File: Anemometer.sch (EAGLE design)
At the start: 30 parts, among them IC1 TINY2313-*S*, IC2 74HC151D, IC3 74HC151D, IC4 74HC08D, IC5 LM555D, IC6 74HC138D, IC7 74ALS04D, IC8 74HC393D, Q1 16MHz

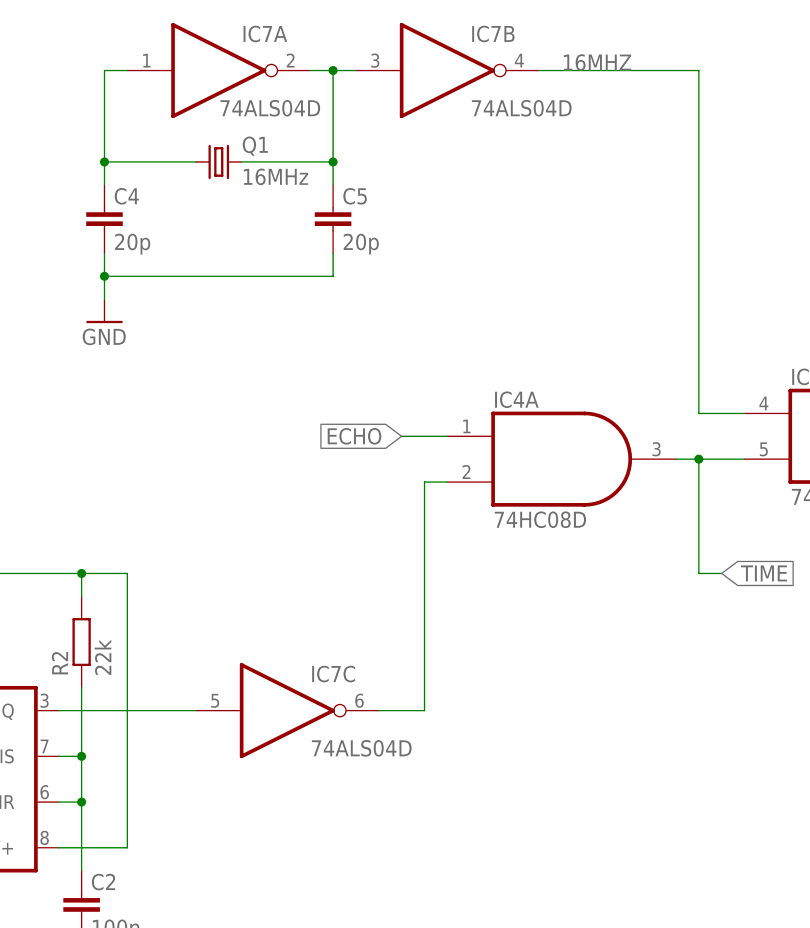
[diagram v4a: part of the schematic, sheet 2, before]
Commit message: added timeout protection
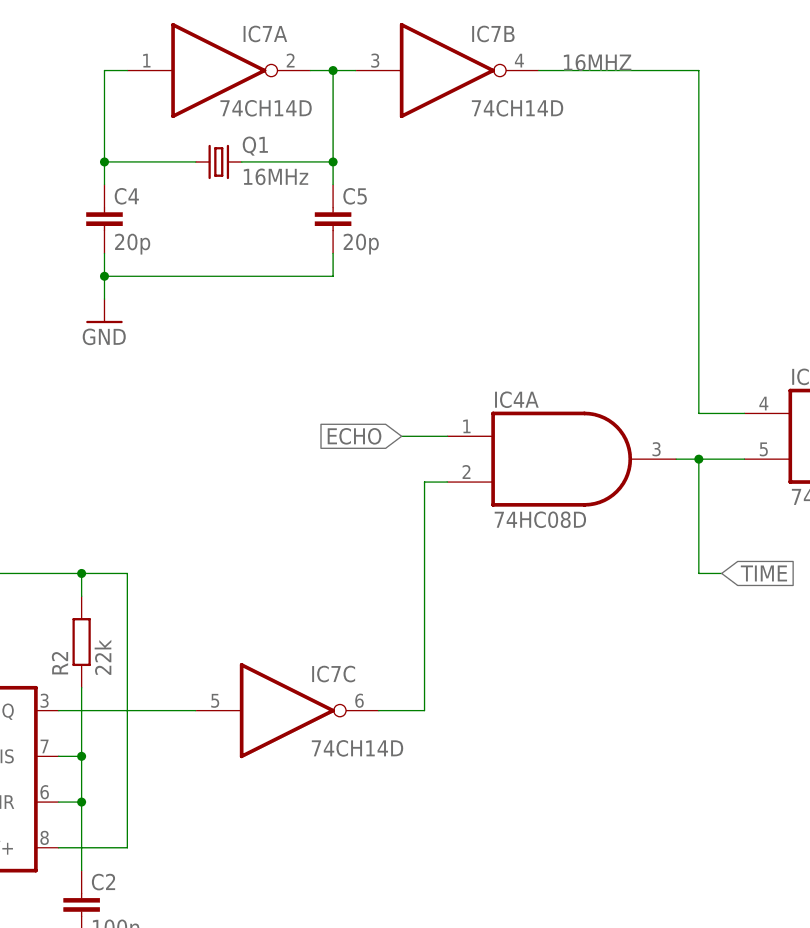
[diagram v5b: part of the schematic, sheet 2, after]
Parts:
- IC7: value 74ALS04D -> 74CH14D
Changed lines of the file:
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@@
 <part name="FRAME4" library="frames" library_urn="urn:adsk.eagle:library:229" deviceset="A4L-LOC" device="" value="Frame"/>
 <part name="IC8" library="74xx-us" library_urn="urn:adsk.eagle:library:88" deviceset="74*393" device="D" package3d_urn="urn:adsk.eagle:package:2917/1" technology="LS" value="74HC393D"/>
-<part name="IC7" library="74xx-us" library_urn="urn:adsk.eagle:library:88" deviceset="74*04" device="D" package3d_urn="urn:adsk.eagle:package:2917/1" technology="ALS"/>
+<part name="IC7" library="74xx-us" library_urn="urn:adsk.eagle:library:88" deviceset="74*04" device="D" package3d_urn="urn:adsk.eagle:package:2917/1" technology="ALS" value="74CH14D"/>
 <part name="P+12" library="supply1" library_urn="urn:adsk.eagle:library:371" deviceset="VCC" device=""/>
 <part name="GND16" library="supply1" library_urn="urn:adsk.eagle:library:371" deviceset="GND" device=""/>

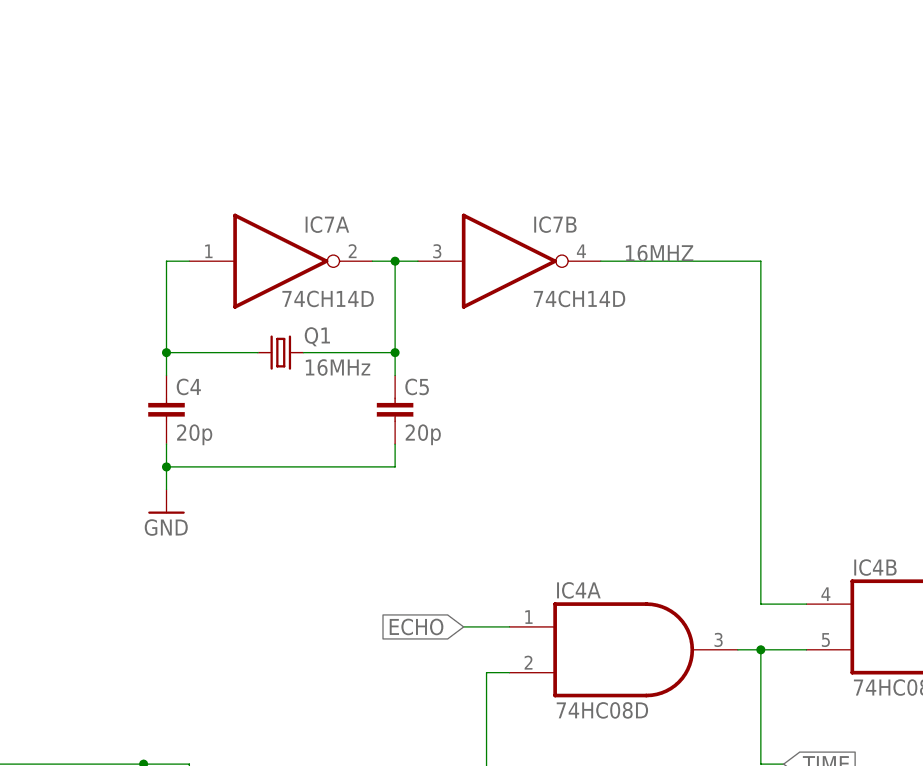
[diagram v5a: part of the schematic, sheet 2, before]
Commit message: added resistors to make clock run reliable
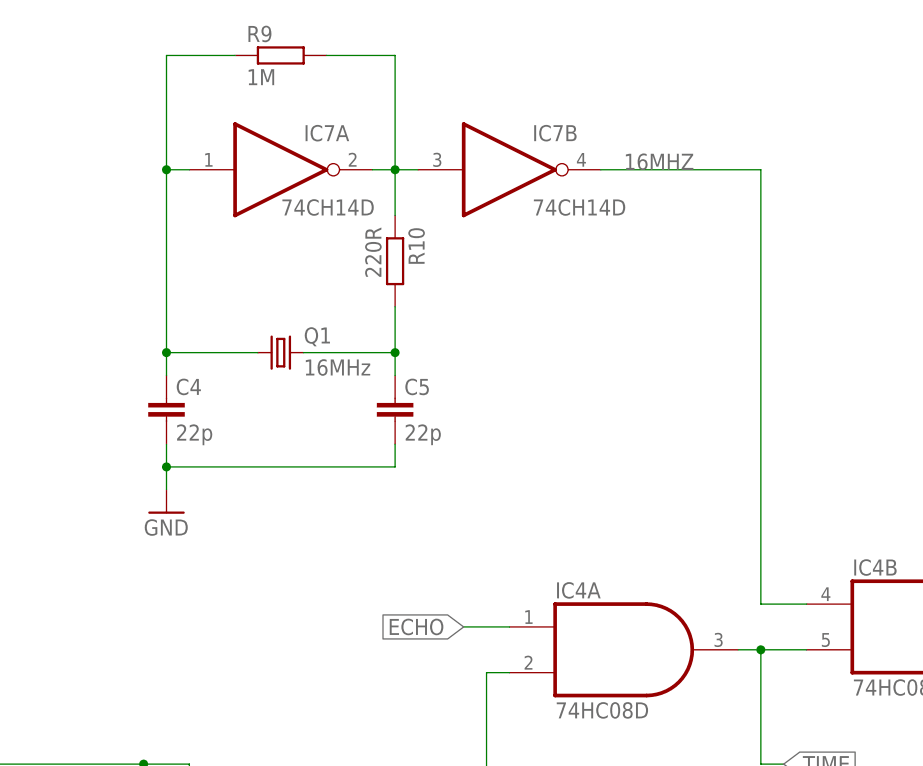
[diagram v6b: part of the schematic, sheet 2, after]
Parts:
- added R10: 220R, rcl:R-EU_R0805
- added R9: 1M, rcl:R-EU_R0805
- C4, C5: value 20p -> 22p
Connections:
- new net N$8: IC7A.O, IC7B.I, R10.1, R9.2
- net N$6: now also R9.1
- net N$7: now also R10.2; no longer IC7A.O, IC7B.I
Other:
- moved on the sheet: IC7A, IC7B
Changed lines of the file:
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@@
 <part name="GND14" library="supply1" library_urn="urn:adsk.eagle:library:371" deviceset="GND" device=""/>
 <part name="Q1" library="crystal" library_urn="urn:adsk.eagle:library:204" deviceset="CRYSTAL" device="HC49UP" package3d_urn="urn:adsk.eagle:package:12078/1" value="16MHz"/>
-<part name="C4" library="rcl" library_urn="urn:adsk.eagle:library:334" deviceset="C-EU" device="C0805" package3d_urn="urn:adsk.eagle:package:23617/2" value="20p"/>
-<part name="C5" library="rcl" library_urn="urn:adsk.eagle:library:334" deviceset="C-EU" device="C0805" package3d_urn="urn:adsk.eagle:package:23617/2" value="20p"/>
+<part name="C4" library="rcl" library_urn="urn:adsk.eagle:library:334" deviceset="C-EU" device="C0805" package3d_urn="urn:adsk.eagle:package:23617/2" value="22p"/>
+<part name="C5" library="rcl" library_urn="urn:adsk.eagle:library:334" deviceset="C-EU" device="C0805" package3d_urn="urn:adsk.eagle:package:23617/2" value="22p"/>
 <part name="GND15" library="supply1" library_urn="urn:adsk.eagle:library:371" deviceset="GND" device=""/>
 <part name="FRAME4" library="frames" library_urn="urn:adsk.eagle:library:229" deviceset="A4L-LOC" device="" value="Frame"/>
@@
 <part name="GND18" library="supply1" library_urn="urn:adsk.eagle:library:371" deviceset="GND" device=""/>
 <part name="GND19" library="supply1" library_urn="urn:adsk.eagle:library:371" deviceset="GND" device=""/>
+<part name="R9" library="rcl" library_urn="urn:adsk.eagle:library:334" deviceset="R-EU_" device="R0805" package3d_urn="urn:adsk.eagle:package:23553/2" value="1M"/>
+<part name="R10" library="rcl" library_urn="urn:adsk.eagle:library:334" deviceset="R-EU_" device="R0805" package3d_urn="urn:adsk.eagle:package:23553/2" value="220R"/>
 </parts>
 <sheets>
@@
 <attribute name="VALUE" x="195.58" y="73.66" size="1.778" layer="96"/>
 </instance>
-<instance part="IC7" gate="A" x="91.44" y="127" smashed="yes">
-<attribute name="NAME" x="93.98" y="130.175" size="1.778" layer="95"/>
-<attribute name="VALUE" x="91.44" y="121.92" size="1.778" layer="96"/>
-</instance>
-<instance part="IC7" gate="B" x="116.84" y="127" smashed="yes">
-<attribute name="NAME" x="119.38" y="130.175" size="1.778" layer="95"/>
-<attribute name="VALUE" x="119.38" y="121.92" size="1.778" layer="96"/>
+<instance part="IC7" gate="A" x="91.44" y="137.16" smashed="yes">
+<attribute name="NAME" x="93.98" y="140.335" size="1.778" layer="95"/>
+<attribute name="VALUE" x="91.44" y="132.08" size="1.778" layer="96"/>
+</instance>
+<instance part="IC7" gate="B" x="116.84" y="137.16" smashed="yes">
+<attribute name="NAME" x="119.38" y="140.335" size="1.778" layer="95"/>
+<attribute name="VALUE" x="119.38" y="132.08" size="1.778" layer="96"/>
 </instance>
 <instance part="IC7" gate="C" x="99.06" y="55.88" smashed="yes">
 <attribute name="NAME" x="101.6" y="59.055" size="1.778" layer="95"/>
 <attribute name="VALUE" x="101.6" y="50.8" size="1.778" layer="96"/>
+</instance>
+<instance part="R9" gate="G$1" x="91.44" y="149.86" smashed="yes">
+<attribute name="NAME" x="87.63" y="151.3586" size="1.778" layer="95"/>
+<attribute name="VALUE" x="87.63" y="146.558" size="1.778" layer="96"/>
+</instance>
+<instance part="R10" gate="G$1" x="104.14" y="127" smashed="yes" rot="R270">
+<attribute name="NAME" x="105.6386" y="130.81" size="1.778" layer="95" rot="R270"/>
+<attribute name="VALUE" x="100.838" y="130.81" size="1.778" layer="96" rot="R270"/>
 </instance>
 </instances>
@@
 <pinref part="IC4" gate="B" pin="I0"/>
 <wire x1="149.86" y1="88.9" x2="144.78" y2="88.9" width="0.1524" layer="91"/>
-<wire x1="127" y1="127" x2="144.78" y2="127" width="0.1524" layer="91"/>
-<wire x1="144.78" y1="127" x2="144.78" y2="88.9" width="0.1524" layer="91"/>
-<label x="129.54" y="127" size="1.778" layer="95"/>
+<wire x1="127" y1="137.16" x2="144.78" y2="137.16" width="0.1524" layer="91"/>
+<wire x1="144.78" y1="137.16" x2="144.78" y2="88.9" width="0.1524" layer="91"/>
+<label x="129.54" y="137.16" size="1.778" layer="95"/>
 <pinref part="IC7" gate="B" pin="O"/>
 </segment>
@@
 <pinref part="C4" gate="G$1" pin="1"/>
 <wire x1="78.74" y1="114.3" x2="78.74" y2="116.84" width="0.1524" layer="91"/>
-<wire x1="78.74" y1="116.84" x2="78.74" y2="127" width="0.1524" layer="91"/>
-<wire x1="78.74" y1="127" x2="81.28" y2="127" width="0.1524" layer="91"/>
+<wire x1="78.74" y1="116.84" x2="78.74" y2="137.16" width="0.1524" layer="91"/>
+<wire x1="78.74" y1="137.16" x2="81.28" y2="137.16" width="0.1524" layer="91"/>
 <pinref part="Q1" gate="G$1" pin="1"/>
 <wire x1="88.9" y1="116.84" x2="78.74" y2="116.84" width="0.1524" layer="91"/>
 <junction x="78.74" y="116.84"/>
 <pinref part="IC7" gate="A" pin="I"/>
+<pinref part="R9" gate="G$1" pin="1"/>
+<wire x1="86.36" y1="149.86" x2="78.74" y2="149.86" width="0.1524" layer="91"/>
+<wire x1="78.74" y1="149.86" x2="78.74" y2="137.16" width="0.1524" layer="91"/>
+<junction x="78.74" y="137.16"/>
 </segment>
 </net>
@@
 <wire x1="93.98" y1="116.84" x2="104.14" y2="116.84" width="0.1524" layer="91"/>
 <wire x1="104.14" y1="116.84" x2="104.14" y2="114.3" width="0.1524" layer="91"/>
-<wire x1="101.6" y1="127" x2="104.14" y2="127" width="0.1524" layer="91"/>
-<wire x1="104.14" y1="127" x2="104.14" y2="116.84" width="0.1524" layer="91"/>
 <junction x="104.14" y="116.84"/>
-<wire x1="106.68" y1="127" x2="104.14" y2="127" width="0.1524" layer="91"/>
-<junction x="104.14" y="127"/>
+<wire x1="104.14" y1="121.92" x2="104.14" y2="116.84" width="0.1524" layer="91"/>
+<pinref part="R10" gate="G$1" pin="2"/>
+</segment>
+</net>
+<net name="N$8" class="0">
+<segment>
 <pinref part="IC7" gate="A" pin="O"/>
+<wire x1="101.6" y1="137.16" x2="104.14" y2="137.16" width="0.1524" layer="91"/>
 <pinref part="IC7" gate="B" pin="I"/>
-</segment>
-</net>
+<wire x1="106.68" y1="137.16" x2="104.14" y2="137.16" width="0.1524" layer="91"/>
+<junction x="104.14" y="137.16"/>
+<wire x1="104.14" y1="137.16" x2="104.14" y2="132.08" width="0.1524" layer="91"/>
+<pinref part="R10" gate="G$1" pin="1"/>
+<pinref part="R9" gate="G$1" pin="2"/>
+<wire x1="96.52" y1="149.86" x2="104.14" y2="149.86" width="0.1524" layer="91"/>
+<wire x1="104.14" y1="149.86" x2="104.14" y2="137.16" width="0.1524" layer="91"/>
+</segment>
+</net>
